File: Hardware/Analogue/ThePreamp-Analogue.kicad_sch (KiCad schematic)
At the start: 31 parts, among them IC1 ULN2803CDWR, J1 To preamp, J2 From preamp, J3 Digital In, J4 Digital Pass Through, J5 Power In, J6 Power Out, J7 ADS1115, J8 Replace, J9 Replace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

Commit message: pcb redesign
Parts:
- IC1: footprint SOIC127P1030X265-20N -> ULN2803:SOIC127P1030X265-20N
- RCA1, RCA2, RCA5, RCA6: footprint Connector_Audio:RCA Connector ALI -> RCA ALI:RCA Connector ALI; symbol Connector:RCA_Connector_ALI -> RCA ALI:RCA_Connector_ALI
- RCA10, RCA3, RCA4, RCA7, RCA8, RCA9: symbol Connector:RCA_Connector_ALI -> RCA ALI:RCA_Connector_ALI
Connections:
- net RELAY1: now also IC1.20 (1C); no longer IC1.17 (4C)
- net RELAY2: now also IC1.19 (2C); no longer IC1.16 (5C)
- net RELAY3: now also IC1.18 (3C); no longer IC1.15 (6C)
- net RELAY4: now also IC1.17 (4C); no longer IC1.14 (7C)
- net RELAY5: now also IC1.16 (5C); no longer IC1.13 (8C)
- new net RELAY6: IC1.15 (6C)
- new net RELAY7: IC1.14 (7C)
- no-connect marks 31 -> 29

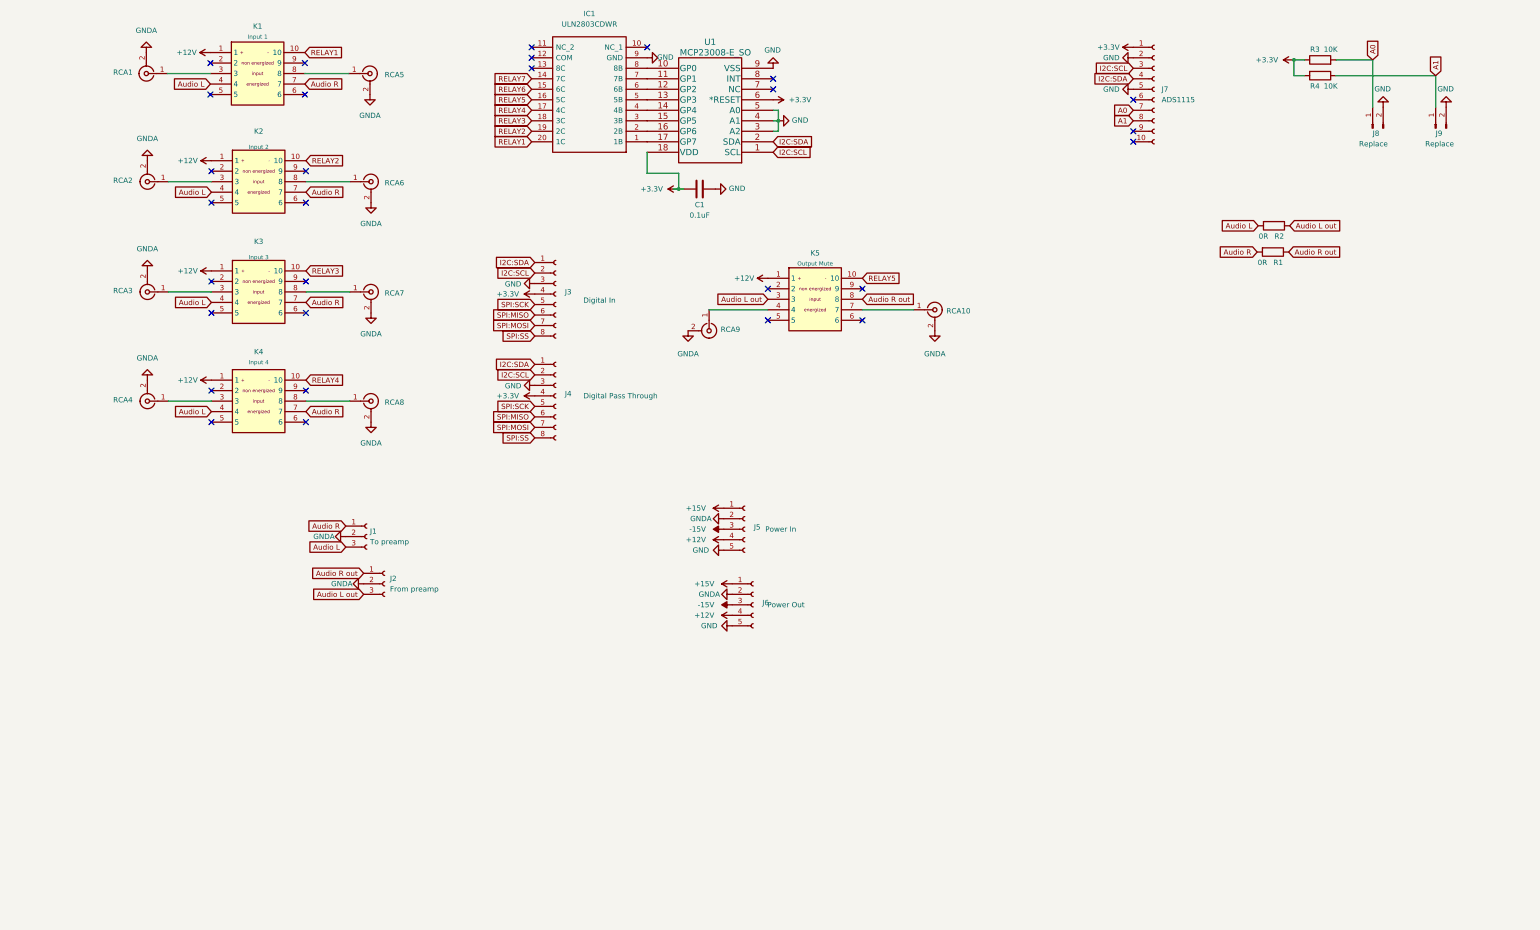
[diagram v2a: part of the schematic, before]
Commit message: Added Trigger functionality (12V and switch)
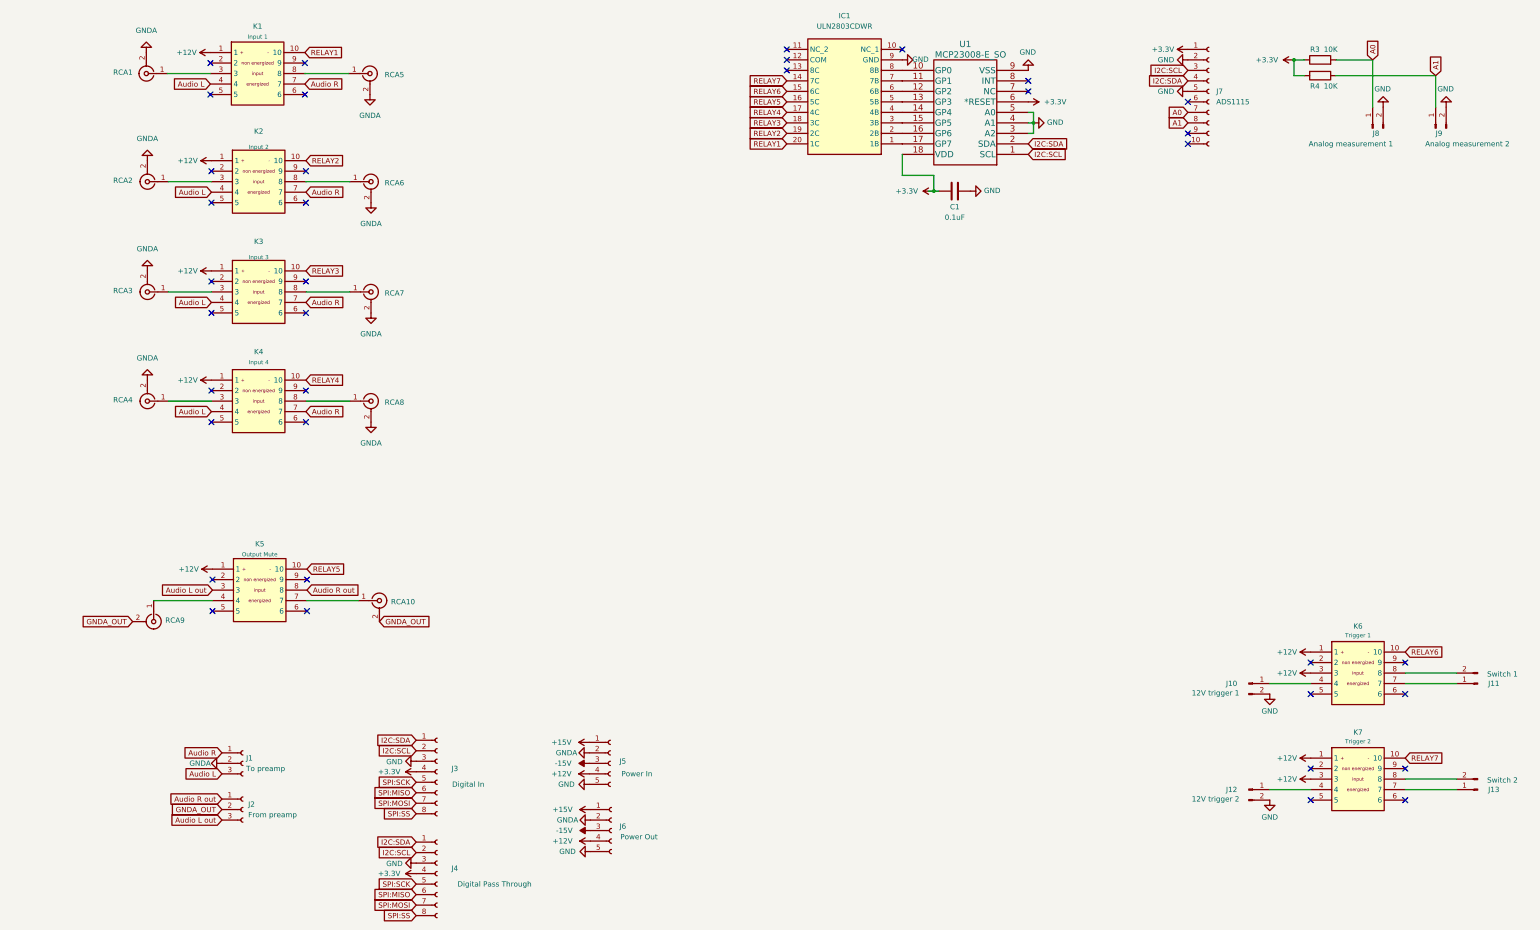
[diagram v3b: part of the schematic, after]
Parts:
- removed R1, R2: 0R, Resistor_THT:R_Axial_DIN0207_L6.3mm_D2.5mm_P7.62mm_Horizontal, symbol Device:R
- added J10: 12V trigger 1, Connector_JST:JST_XH_B2B-XH-A_1x02_P2.50mm_Vertical, symbol Connector:Conn_01x02_Male
- added J11: Switch 1, Connector_JST:JST_XH_B2B-XH-A_1x02_P2.50mm_Vertical, symbol Connector:Conn_01x02_Male
- added J12: 12V trigger 2, Connector_JST:JST_XH_B2B-XH-A_1x02_P2.50mm_Vertical, symbol Connector:Conn_01x02_Male
- added J13: Switch 2, Connector_JST:JST_XH_B2B-XH-A_1x02_P2.50mm_Vertical, symbol Connector:Conn_01x02_Male
- added K6: Trigger 1, EA2-12NJ:DIPS762W60P254L1420H630Q10N, symbol EA2-12NJ:EA2-12NJ
- added K7: Trigger 2, EA2-12NJ:DIPS762W60P254L1420H630Q10N, symbol EA2-12NJ:EA2-12NJ
- J8: value Replace -> Analog measurement 1
- J9: value Replace -> Analog measurement 2
- RCA10, RCA3, RCA4, RCA7, RCA8, RCA9: footprint Connector_Audio:RCA Connector ALI -> RCA ALI:RCA Connector ALI
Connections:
- net +12V: now also K6.1, K6.3, K7.1, K7.3
- net GND: now also J10.2 (Pin_2), J12.2 (Pin_2)
- net GNDA: no longer J2.2 (Pin_2), RCA10.2 (Ext), RCA9.2 (Ext)
- net RELAY6: now also K6.10
- net RELAY7: now also K7.10
- net +3V3 renamed +3.3V
- new net: J12.1 (Pin_1), K7.4
- new net: J13.1 (Pin_1), K7.7
- new net: J13.2 (Pin_2), K7.8
- new net: J11.1 (Pin_1), K6.7
- new net: J11.2 (Pin_2), K6.8
- new net: J10.1 (Pin_1), K6.4
- new net GNDA_OUT: J2.2 (Pin_2), RCA10.2 (Ext), RCA9.2 (Ext)
- no-connect marks 29 -> 37
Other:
- moved on the sheet: C1, J1, J2, J3, J4, J5, J6, J7, K5, RCA10, RCA9, U1

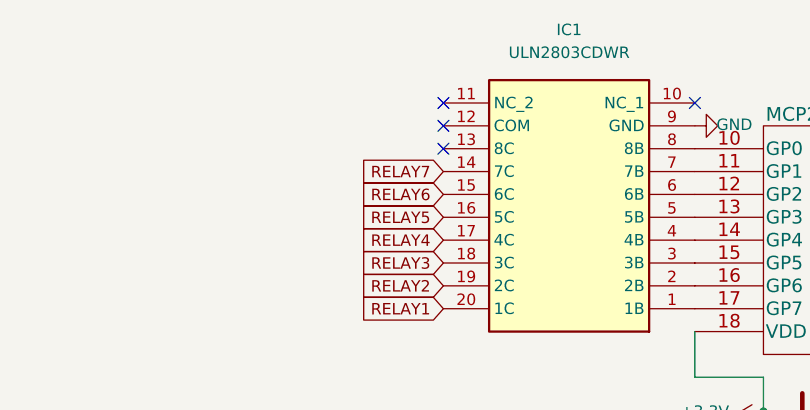
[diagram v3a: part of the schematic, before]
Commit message: Added +12V to COM on ULN2803 (common fly back diode)
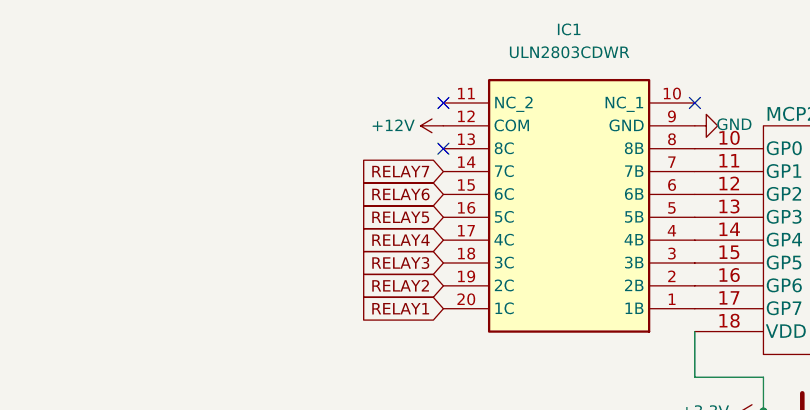
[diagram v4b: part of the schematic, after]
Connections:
- net +12V: now also IC1.12 (COM)
- no-connect marks 37 -> 36
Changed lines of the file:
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@@
   (no_connect (at 86.614 181.61))
   (no_connect (at 329.438 201.676))
-  (no_connect (at 202.692 55.88))
   (no_connect (at 352.298 201.676))
   (no_connect (at 63.246 64.262))
@@
         )
       )
+    )
+  )
+  (symbol (lib_id "power:+12V") (at 202.692 55.88 90) (unit 1)
+    (in_bom yes) (on_board yes) (dnp no) (fields_autoplaced)
+    (property "Reference" "#PWR026" (at 206.502 55.88 0)
+      (effects (font (size 1.27 1.27)) hide)
+    )
+    (property "Value" "+12V" (at 199.517 55.88 90)
+      (effects (font (size 1.27 1.27)) (justify left))
+    )
+    (property "Footprint" "" (at 202.692 55.88 0)
+      (effects (font (size 1.27 1.27)) hide)
+    )
+    (property "Datasheet" "" (at 202.692 55.88 0)
+      (effects (font (size 1.27 1.27)) hide)
+    )
+    (pin "1")
+    (instances
+      (project "ThePreamp-Analogue"
+        (path "/f6c644f4-3036-41a6-9e14-2c08c079c6cd"
+          (reference "#PWR026") (unit 1)
+        )
+      )

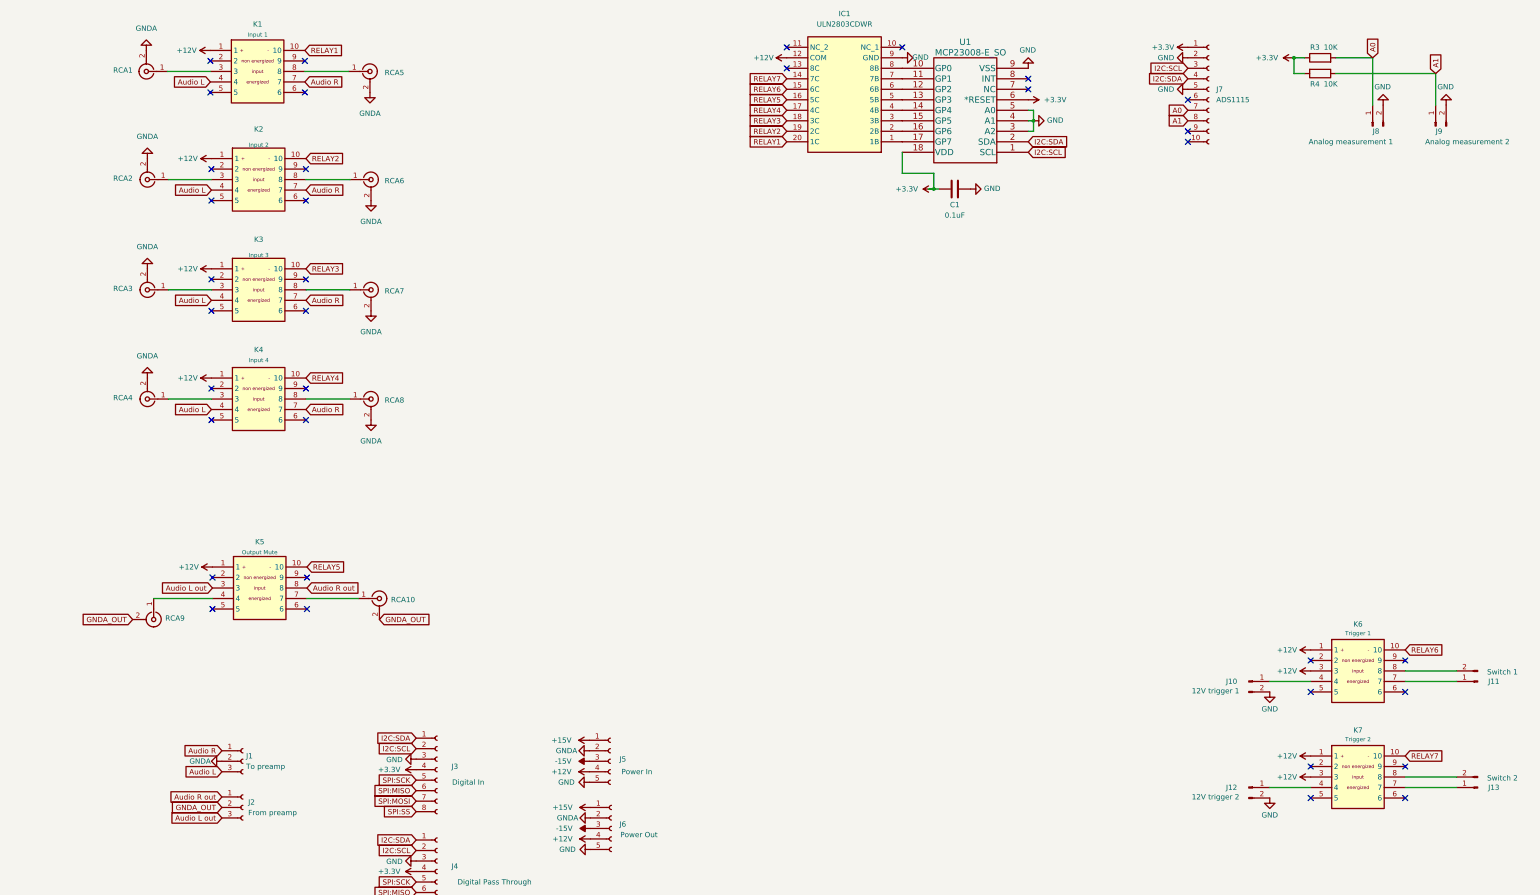
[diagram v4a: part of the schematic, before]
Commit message: v1.1 - added internal input and IDC for switches etc
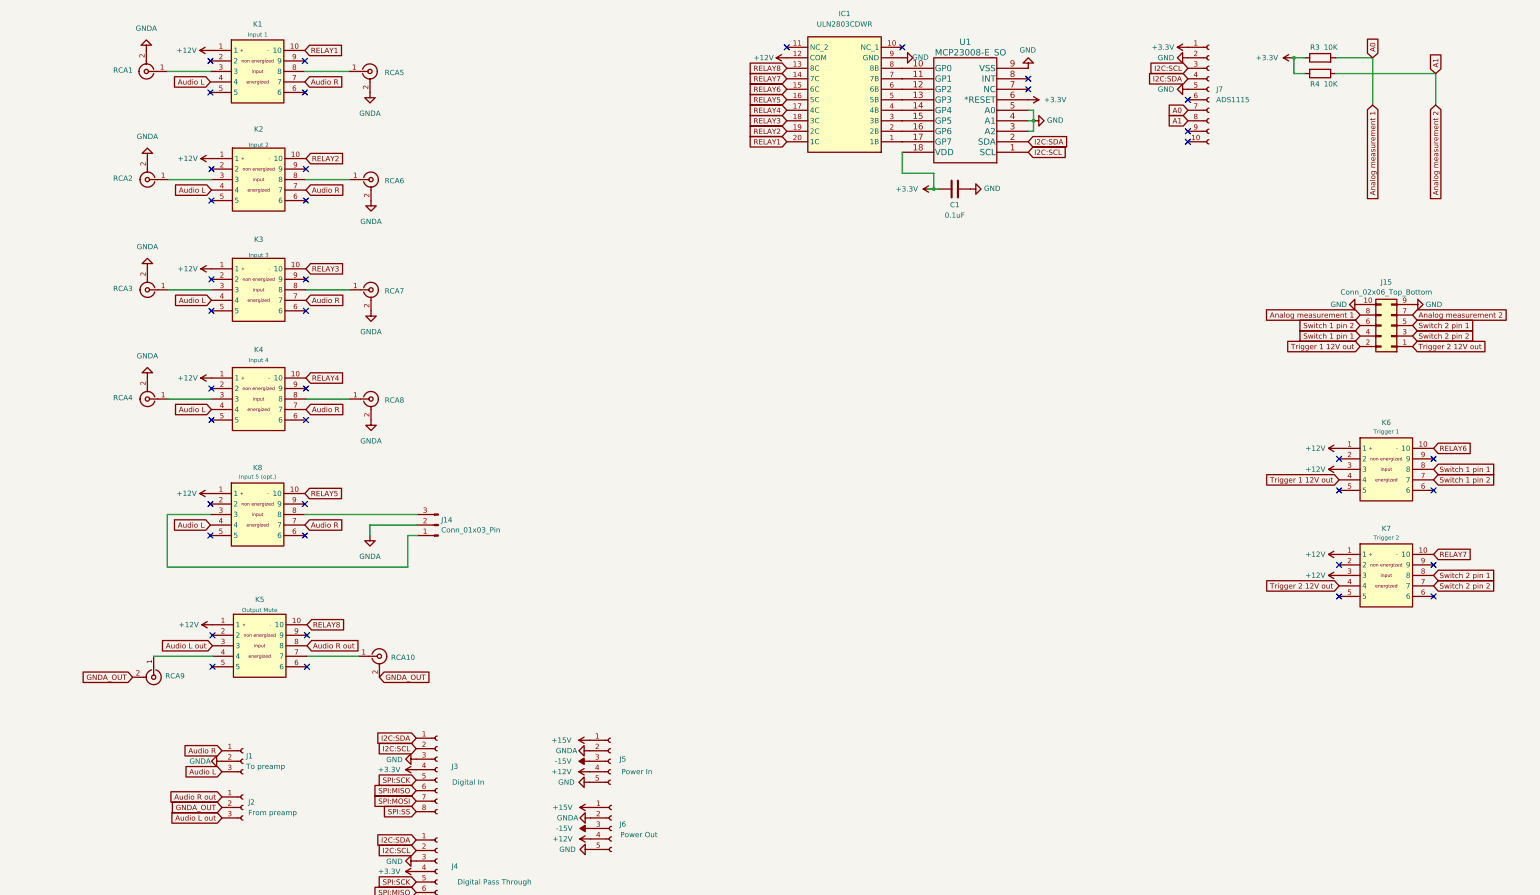
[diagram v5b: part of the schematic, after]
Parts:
- removed J10: 12V trigger 1, Connector_JST:JST_XH_B2B-XH-A_1x02_P2.50mm_Vertical, symbol Connector:Conn_01x02_Male
- removed J11: Switch 1, Connector_JST:JST_XH_B2B-XH-A_1x02_P2.50mm_Vertical, symbol Connector:Conn_01x02_Male
- removed J12: 12V trigger 2, Connector_JST:JST_XH_B2B-XH-A_1x02_P2.50mm_Vertical, symbol Connector:Conn_01x02_Male
- removed J13: Switch 2, Connector_JST:JST_XH_B2B-XH-A_1x02_P2.50mm_Vertical, symbol Connector:Conn_01x02_Male
- removed J8: Analog measurement 1, Connector_JST:JST_XH_B2B-XH-A_1x02_P2.50mm_Vertical, symbol Connector:Conn_01x02_Male
- removed J9: Analog measurement 2, Connector_JST:JST_XH_B2B-XH-A_1x02_P2.50mm_Vertical, symbol Connector:Conn_01x02_Male
- added J14: Conn_01x03_Pin, Connector_PinHeader_2.54mm:PinHeader_1x03_P2.54mm_Vertical, symbol Connector:Conn_01x03_Pin
- added J15: Conn_02x06_Top_Bottom, Connector_IDC:IDC-Header_2x05_P2.54mm_Vertical, symbol Connector_Generic:Conn_02x05_Odd_Even
- added K8: Input 5 (opt.), EA2-12NJ:DIPS762W60P254L1420H630Q10N, symbol EA2-12NJ:EA2-12NJ
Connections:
- net +12V: now also K8.1
- net A0: now also J15.8 (Pin_8)
- net A1: now also J15.7 (Pin_7)
- net Audio L: now also K8.4
- net Audio R: now also K8.7
- net GND: now also J15.10 (Pin_10), J15.9 (Pin_9)
- net GNDA: now also J14.2 (Pin_2)
- net RELAY5: now also K8.10; no longer K5.10
- net Trigger 2 12V out: now reaches K7.4
- net Trigger 2 12V out: now also J15.1 (Pin_1)
- net Switch 2 pin 2: now reaches K7.7
- net Switch 2 pin 2: now also J15.3 (Pin_3)
- net Switch 2 pin 1: now reaches K7.8
- net Switch 2 pin 1: now also J15.5 (Pin_5)
- net Switch 1 pin 2: now reaches K6.7
- net Switch 1 pin 2: now also J15.6 (Pin_6)
- net Switch 1 pin 1: now reaches K6.8
- net Switch 1 pin 1: now also J15.4 (Pin_4)
- net Trigger 1 12V out: now reaches K6.4
- net Trigger 1 12V out: now also J15.2 (Pin_2)
- net RELAY8: now reaches IC1.13 (8C)
- net RELAY8: now also K5.10
- new net: J14.1 (Pin_1), K8.3
- new net: J14.3 (Pin_3), K8.8
- no-connect marks 36 -> 39
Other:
- moved on the sheet: K5, K6, K7, RCA10, RCA9
